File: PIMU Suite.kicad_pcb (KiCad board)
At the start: 2 copper layers, 65.5 x 48.5 mm, 5 parts, among them J1 Conn_01x05, U1 Teensy4.1, U2 MICROSD_SPI_OR_SDIO_CARD

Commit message: hand-routed
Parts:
- moved J1 58.6 mm to (113.5, 74.5), turned to 90 degrees
- moved IMU1 3.77 mm to (149.4, 109.0), turned to 180 degrees
- turned U2 to 180 degrees
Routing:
- net Net-(J1-Pin_1): track 81.3 -> 5.33 mm, vias 1 -> 0
- net Net-(J1-Pin_2): track 63.2 -> 4.69 mm
- net /SD_SCK: track 68.9 -> 28.3 mm
- net Net-(IMU1-SDA): track 53.6 -> 29.5 mm, vias 1 -> 2
- net /SD_MISO: track 44.1 -> 21.6 mm, vias 1 -> 0
- net Net-(IMU1-GND): track 65.0 -> 46.0 mm
- net Net-(IMU1-VIN): track 72.5 -> 58.1 mm, vias 0 -> 1
- net /SD_MOSI: track 34.3 -> 21.6 mm
- net Net-(IMU1-SCL): track 43.3 -> 32.0 mm, vias 0 -> 2
- net /SD_CS: track 28.9 -> 21.6 mm
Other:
- board size 65.5 x 48.5 mm -> 65 x 50.5 mm

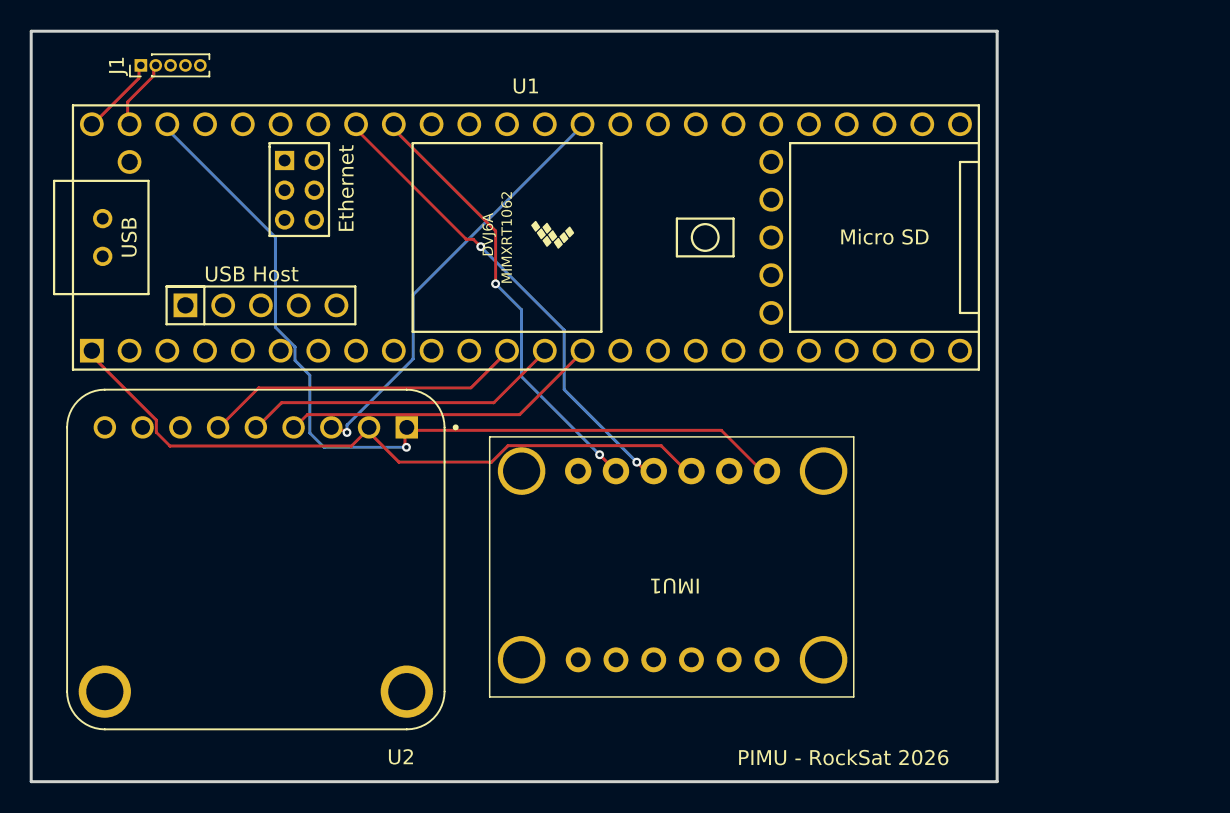
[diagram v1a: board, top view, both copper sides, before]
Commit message: added pressure
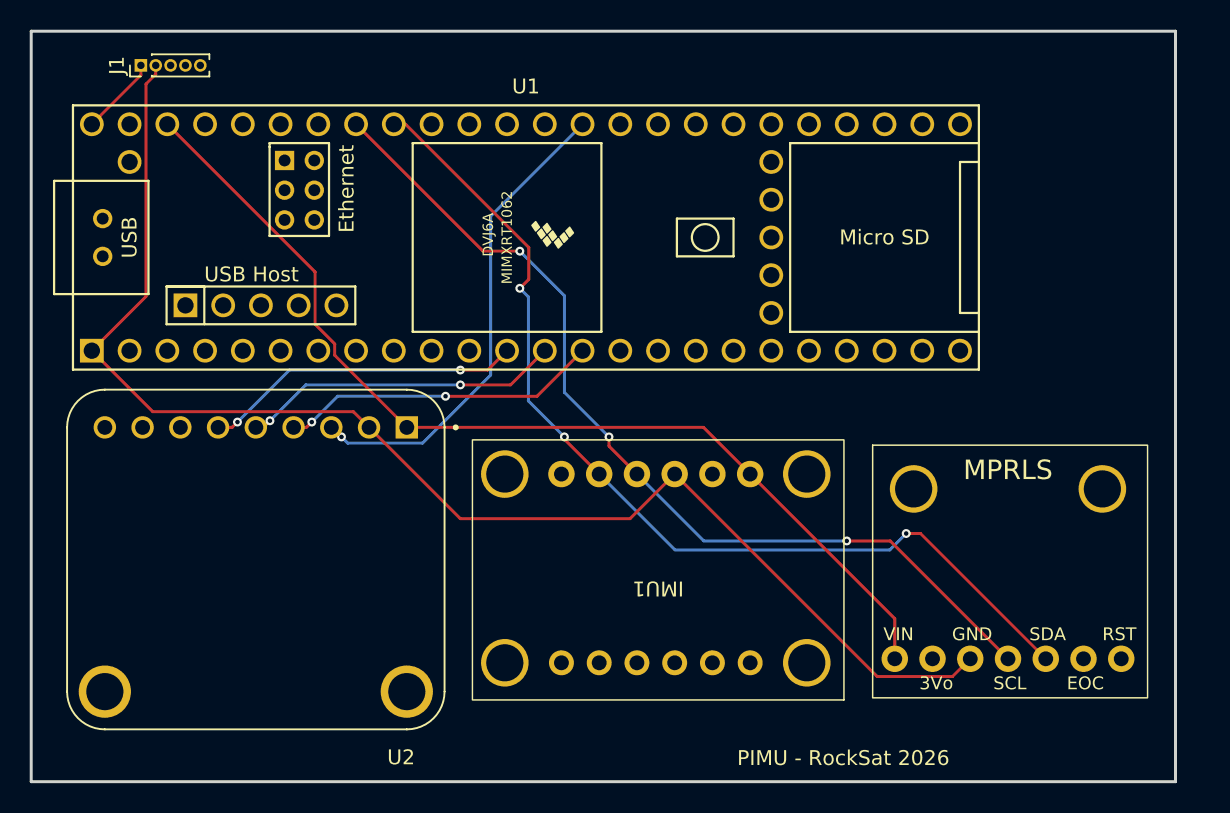
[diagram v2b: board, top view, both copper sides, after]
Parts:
- added PRESSURE1: MPRLS, RSX:MPRLS_Pressure, F.Cu at (172.2, 107.6)
- moved IMU1 1.15 mm to (148.3, 109.2)
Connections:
- J1 pad 2: Net-(J1-Pin_2) -> Net-(IMU1-GND)
- U1 pad 47: Net-(J1-Pin_2) -> unconnected-(U1-GND-Pad47)
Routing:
- net Net-(IMU1-GND): track 46.0 -> 92.2 mm
- net Net-(IMU1-SDA): track 29.5 -> 66.3 mm, vias 2 -> 3
- net Net-(IMU1-SCL): track 32.0 -> 62.9 mm, vias 2 -> 3
- net Net-(IMU1-VIN): track 58.1 -> 67.9 mm, vias 1 -> 0
- net Net-(J1-Pin_2): track 4.69 -> 0.00 mm
- net /SD_SCK: track 28.3 -> 32.5 mm
- net /SD_MISO: vias 0 -> 2
- net /SD_MOSI: vias 0 -> 2
- net /SD_CS: vias 0 -> 2
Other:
- board size 65 x 50.5 mm -> 77 x 50.5 mm

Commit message: Using new pressure sensor
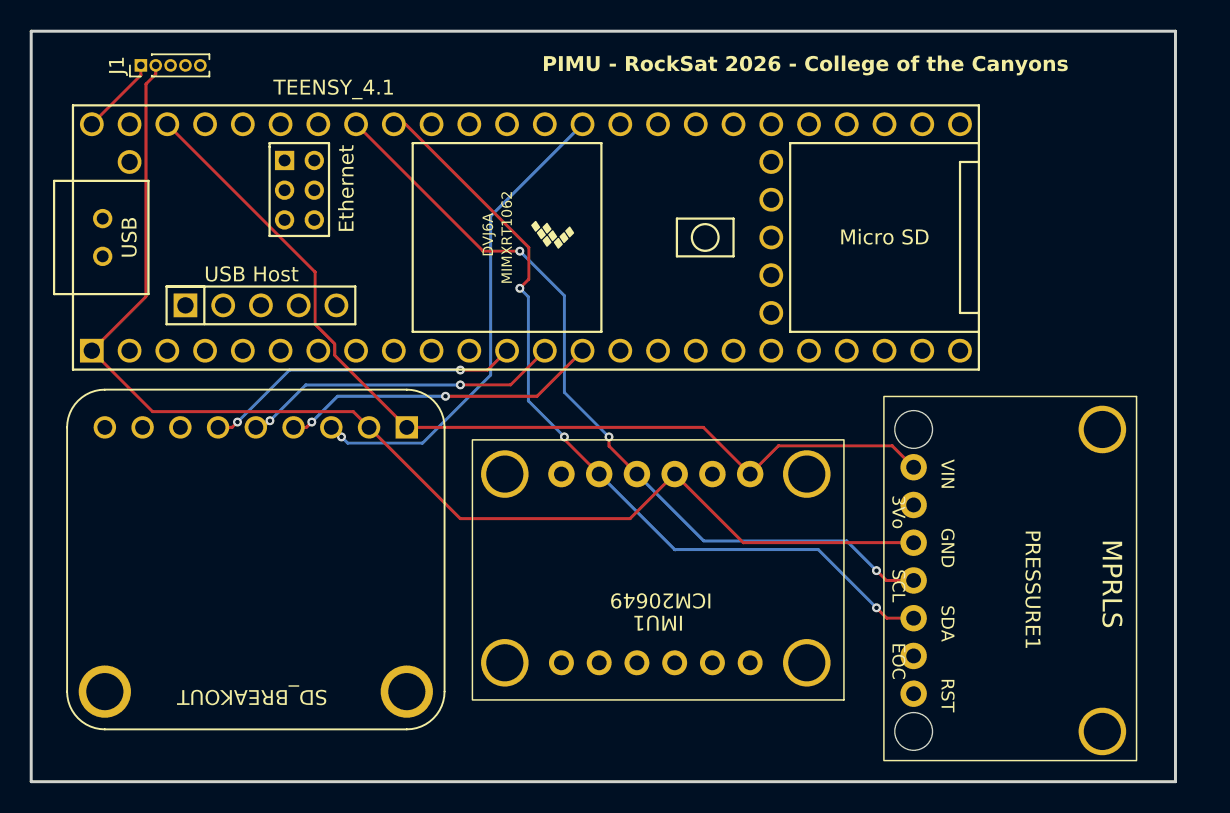
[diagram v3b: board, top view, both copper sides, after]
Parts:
- PRESSURE1: footprint RSX:MPRLS_Pressure -> RSX:BMP280
- moved PRESSURE1 2.35 mm to (173.0, 109.8), turned to -90 degrees
- renumbered U2 to SD_BREAKOUT, U1 to TEENSY_4.1
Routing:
- net Net-(IMU1-SDA): track 66.3 -> 55.4 mm
- net Net-(IMU1-SCL): track 62.9 -> 54.4 mm
- net Net-(IMU1-GND): track 92.2 -> 84.1 mm
- net Net-(IMU1-VIN): track 67.9 -> 63.9 mm
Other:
- board text added: "PIMU - RockSat 2026 - College of the Canyons"
- board text removed: "PIMU - RockSat 2026"

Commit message: Actually use correct sensor
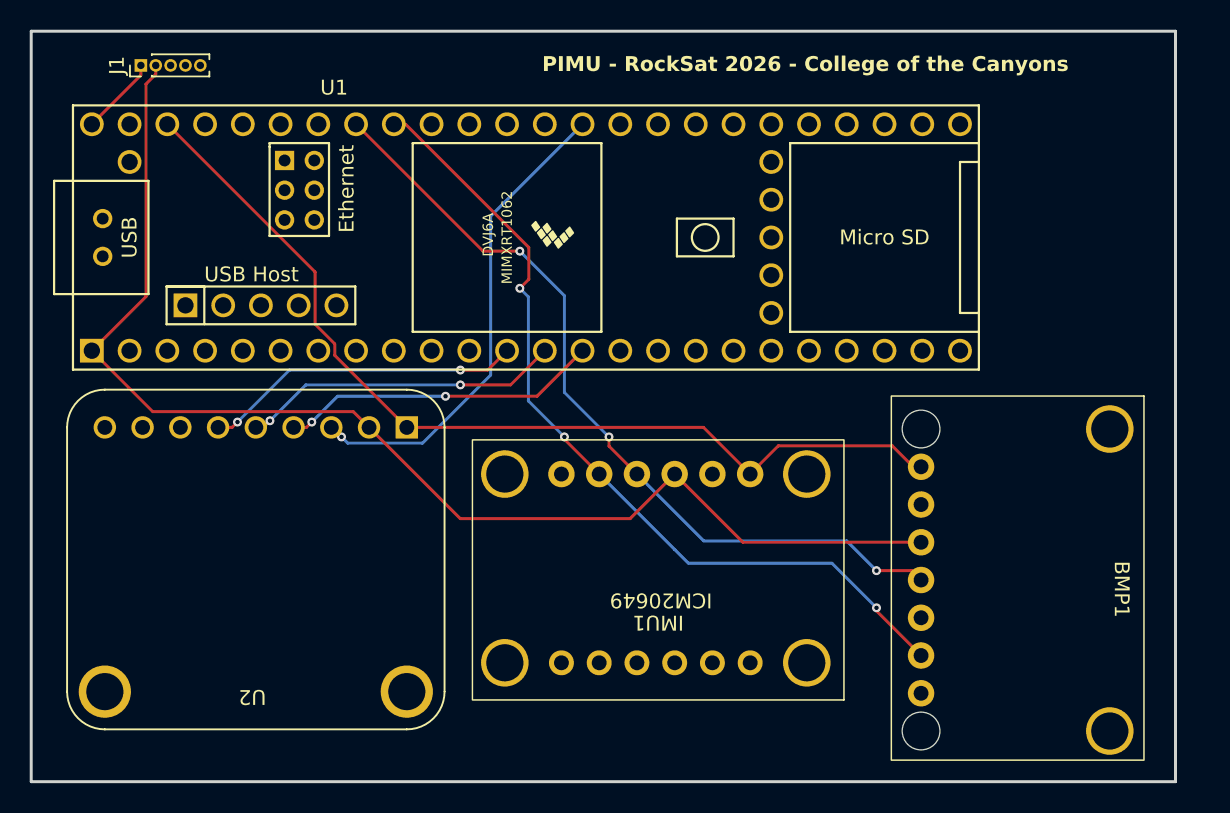
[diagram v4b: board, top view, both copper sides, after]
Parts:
- removed PRESSURE1: MPRLS, RSX:BMP280
- added BMP1: BMP280, RSX:BMP280, F.Cu at (173.5, 109.8)
- renumbered TEENSY_4.1 to U1, SD_BREAKOUT to U2
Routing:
- net Net-(BMP1-SDI): track 55.4 -> 57.1 mm
